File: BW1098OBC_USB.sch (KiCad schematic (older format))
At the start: 53 parts, among them J10 USB3.1 TYPEC 24P SMD RA, U5 USB Type-C Switch, U6 USB Type-C Port Control

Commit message: Update
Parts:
- C?: renamed from C31; symbol BW1098OBC_USB-SchDoc-rescue:GRM033R61A104KE15D- -> BW1098OBC_USB-cache:GRM033R61A104KE15D
- C?: renamed from C32; symbol BW1098OBC_USB-SchDoc-rescue:GRM033R61A104KE15D- -> BW1098OBC_USB-cache:GRM033R61A104KE15D
- C?: renamed from C33; symbol BW1098OBC_USB-SchDoc-rescue:GRM033R61A104KE15D- -> BW1098OBC_USB-cache:GRM033R61A104KE15D
- C?: renamed from C34; symbol BW1098OBC_USB-SchDoc-rescue:GRM033R61A104KE15D- -> BW1098OBC_USB-cache:GRM033R61A104KE15D
- C?: renamed from C36; symbol BW1098OBC_USB-SchDoc-rescue:GRM155R60J106ME15D- -> BW1098OBC_Power_Supply-cache:BW1098OBC_Power_Supply-SchDoc-rescue_GRM188R61A226ME15D-
- C?: renamed from C35; symbol BW1098OBC_USB-SchDoc-rescue:GRM155R60J106ME15D- -> BW1098OBC_Power_Supply-cache:BW1098OBC_Power_Supply-SchDoc-rescue_GRM188R61A226ME15D-
- C?: renamed from C29; symbol BW1098OBC_USB-SchDoc-rescue:GRM155R60J106ME15D- -> BW1098OBC_Power_Supply-cache:BW1098OBC_Power_Supply-SchDoc-rescue_GRM188R61A226ME15D-
- C?: renamed from C30; symbol BW1098OBC_USB-SchDoc-rescue:GRM155R60J106ME15D- -> BW1098OBC_Power_Supply-cache:BW1098OBC_Power_Supply-SchDoc-rescue_GRM188R61A226ME15D-
- J?: renamed from J10; symbol BW1098OBC_USB-SchDoc-rescue:105450-0101- -> BW1098OBC_USB-cache:105450-0101
- R?: renamed from R11; symbol BW1098OBC_USB-SchDoc-rescue:RC0402FR-1310KL- -> BW1098OBC_IMX378-rescue:RC0402FR-1310KL--BW1098OBC_IMX378-SchDoc-rescue
- R?: renamed from R12; symbol BW1098OBC_USB-SchDoc-rescue:RC0402FR-1310KL- -> BW1098OBC_IMX378-rescue:RC0402FR-1310KL--BW1098OBC_IMX378-SchDoc-rescue
- R?: renamed from R16; symbol BW1098OBC_USB-SchDoc-rescue:RC0402FR-1310KL- -> BW1098OBC_IMX378-rescue:RC0402FR-1310KL--BW1098OBC_IMX378-SchDoc-rescue
- R?: renamed from R14; symbol BW1098OBC_USB-SchDoc-rescue:RC0402FR-1310KL- -> BW1098OBC_IMX378-rescue:RC0402FR-1310KL--BW1098OBC_IMX378-SchDoc-rescue
- R?: renamed from R13; symbol BW1098OBC_USB-SchDoc-rescue:RC0402FR-1310KL- -> BW1098OBC_IMX378-rescue:RC0402FR-1310KL--BW1098OBC_IMX378-SchDoc-rescue
- R?: renamed from R21; symbol BW1098OBC_USB-SchDoc-rescue:RC0402FR-1310KL- -> BW1098OBC_IMX378-rescue:RC0402FR-1310KL--BW1098OBC_IMX378-SchDoc-rescue
- R?: renamed from R20; symbol BW1098OBC_USB-SchDoc-rescue:RC0402FR-1310KL- -> BW1098OBC_IMX378-rescue:RC0402FR-1310KL--BW1098OBC_IMX378-SchDoc-rescue
- R?: renamed from R19; symbol BW1098OBC_USB-SchDoc-rescue:RC0402FR-1310KL- -> BW1098OBC_IMX378-rescue:RC0402FR-1310KL--BW1098OBC_IMX378-SchDoc-rescue
- R?: renamed from R15; symbol BW1098OBC_USB-SchDoc-rescue:CRCW04021M80FKED- -> BW1098OBC_USB-cache:CRCW04021M80FKED
- R?: renamed from R17; symbol BW1098OBC_USB-SchDoc-rescue:CRCW04021M80FKED- -> BW1098OBC_USB-cache:CRCW04021M80FKED
- R?: renamed from R18; symbol BW1098OBC_USB-SchDoc-rescue:RC0402FR-1310KL- -> BW1098OBC_IMX378-rescue:RC0402FR-1310KL--BW1098OBC_IMX378-SchDoc-rescue
- TP?: renamed from TP23; value (none) -> ~; symbol BW1098OBC_USB-SchDoc-rescue:TEST_POINT- -> BW1098OBC_Power_Supply-cache:BW1098OBC_Power_Supply-SchDoc-rescue_TEST_POINT-
- TP?: renamed from TP22; value (none) -> ~; symbol BW1098OBC_USB-SchDoc-rescue:TEST_POINT- -> BW1098OBC_Power_Supply-cache:BW1098OBC_Power_Supply-SchDoc-rescue_TEST_POINT-
- TP?: renamed from TP21; value (none) -> ~; symbol BW1098OBC_USB-SchDoc-rescue:TEST_POINT- -> BW1098OBC_Power_Supply-cache:BW1098OBC_Power_Supply-SchDoc-rescue_TEST_POINT-
- TP?: renamed from TP19; value (none) -> ~; symbol BW1098OBC_USB-SchDoc-rescue:TEST_POINT- -> BW1098OBC_Power_Supply-cache:BW1098OBC_Power_Supply-SchDoc-rescue_TEST_POINT-
- U?: renamed from U5; symbol BW1098OBC_USB-SchDoc-rescue:HD3SS3212RKSR- -> BW1098OBC_USB-cache:HD3SS3212RKSR
- U?: renamed from U6; symbol BW1098OBC_USB-SchDoc-rescue:TUSB321RWBR- -> BW1098OBC_USB-cache:TUSB321RWBR
- renumbered 3V3_5 to 3V3_?, 3V3_4 to 3V3_?, 3V3_3 to 3V3_?, GND_88 to GND_?, GND_87 to GND_?, GND_86 to GND_?, GND_85 to GND_?, GND_84 to GND_?, GND_83 to GND_?, GND_82 to GND_?, GND_81 to GND_?, GND_80 to GND_?, GND_79 to GND_?, GND_78 to GND_?, GND_77 to GND_?, GND_76 to GND_?, GND_75 to GND_?, GND_74 to GND_?, VBUS_10 to VBUS_?, VBUS_9 to VBUS_?, VBUS_8 to VBUS_?, VBUS_7 to VBUS_?, VBUS_6 to VBUS_?, VBUS_5 to VBUS_?, VDD_5V_19 to VDD_5V_?, VDD_5V_18 to VDD_5V_?, VDD_5V_17 to VDD_5V_?
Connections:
- wire segments 138 -> 142

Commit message: Cleaned up some duplicates, started reorganizing and putting symbols into one luxonis library so the others can be deleted, added SOM Connector footprint
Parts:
- R? (x9): symbol BW1098OBC_IMX378-rescue:RC0402FR-1310KL--BW1098OBC_IMX378-SchDoc-rescue -> BW1098OBC_TopLevel-rescue:RC0402FR-1310KL--BW1098OBC_IMX378-SchDoc-rescue-BW1098OBC_IMX378-rescue
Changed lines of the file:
@@
 Connection ~ 13300 7600
 $Comp
-L BW1098OBC_IMX378-rescue:RC0402FR-1310KL--BW1098OBC_IMX378-SchDoc-rescue R?
+L BW1098OBC_TopLevel-rescue:RC0402FR-1310KL--BW1098OBC_IMX378-SchDoc-rescue-BW1098OBC_IMX378-rescue R?
 U 1 1 5FD52F8D
 P 12400 7300
@@
 $EndComp
 $Comp
-L BW1098OBC_IMX378-rescue:RC0402FR-1310KL--BW1098OBC_IMX378-SchDoc-rescue R?
+L BW1098OBC_TopLevel-rescue:RC0402FR-1310KL--BW1098OBC_IMX378-SchDoc-rescue-BW1098OBC_IMX378-rescue R?
 U 1 1 5FD52F82
 P 12400 7400
@@
 $EndComp
 $Comp
-L BW1098OBC_IMX378-rescue:RC0402FR-1310KL--BW1098OBC_IMX378-SchDoc-rescue R?
+L BW1098OBC_TopLevel-rescue:RC0402FR-1310KL--BW1098OBC_IMX378-SchDoc-rescue-BW1098OBC_IMX378-rescue R?
 U 1 1 5FD52F7A
 P 12400 7600
@@
 $EndComp
 $Comp
-L BW1098OBC_IMX378-rescue:RC0402FR-1310KL--BW1098OBC_IMX378-SchDoc-rescue R?
+L BW1098OBC_TopLevel-rescue:RC0402FR-1310KL--BW1098OBC_IMX378-SchDoc-rescue-BW1098OBC_IMX378-rescue R?
 U 1 1 5FD52F79
 P 12400 7700
@@
 $EndComp
 $Comp
-L BW1098OBC_IMX378-rescue:RC0402FR-1310KL--BW1098OBC_IMX378-SchDoc-rescue R?
+L BW1098OBC_TopLevel-rescue:RC0402FR-1310KL--BW1098OBC_IMX378-SchDoc-rescue-BW1098OBC_IMX378-rescue R?
 U 1 1 5FD52F78
 P 12400 6000
@@
 $EndComp
 $Comp
-L BW1098OBC_IMX378-rescue:RC0402FR-1310KL--BW1098OBC_IMX378-SchDoc-rescue R?
+L BW1098OBC_TopLevel-rescue:RC0402FR-1310KL--BW1098OBC_IMX378-SchDoc-rescue-BW1098OBC_IMX378-rescue R?
 U 1 1 5FD52F77
 P 12400 6600
@@
 $EndComp
 $Comp
-L BW1098OBC_IMX378-rescue:RC0402FR-1310KL--BW1098OBC_IMX378-SchDoc-rescue R?
+L BW1098OBC_TopLevel-rescue:RC0402FR-1310KL--BW1098OBC_IMX378-SchDoc-rescue-BW1098OBC_IMX378-rescue R?
 U 1 1 5FD52F76
 P 12400 6700
@@
 $EndComp
 $Comp
-L BW1098OBC_IMX378-rescue:RC0402FR-1310KL--BW1098OBC_IMX378-SchDoc-rescue R?
+L BW1098OBC_TopLevel-rescue:RC0402FR-1310KL--BW1098OBC_IMX378-SchDoc-rescue-BW1098OBC_IMX378-rescue R?
 U 1 1 5FD52F75
 P 11400 5000
@@
 $EndComp
 $Comp
-L BW1098OBC_IMX378-rescue:RC0402FR-1310KL--BW1098OBC_IMX378-SchDoc-rescue R?
+L BW1098OBC_TopLevel-rescue:RC0402FR-1310KL--BW1098OBC_IMX378-SchDoc-rescue-BW1098OBC_IMX378-rescue R?
 U 1 1 5FD52F74
 P 4300 1400

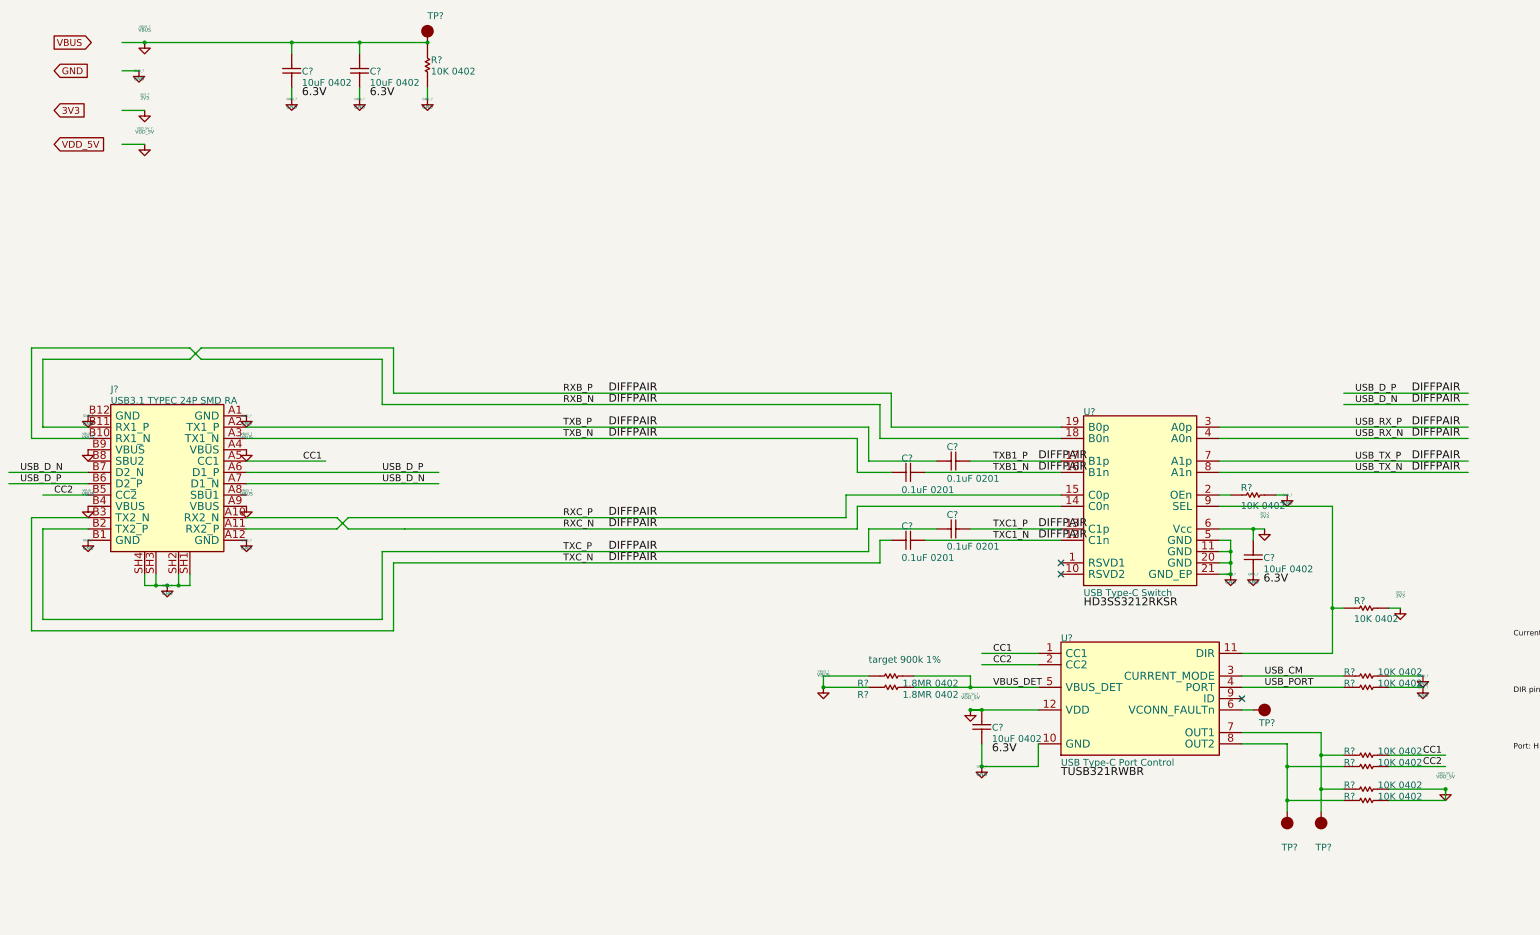
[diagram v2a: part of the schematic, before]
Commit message: More deletion of corrupted or duplicate files, added footprints and associations for mounting holes and 30 pin connector
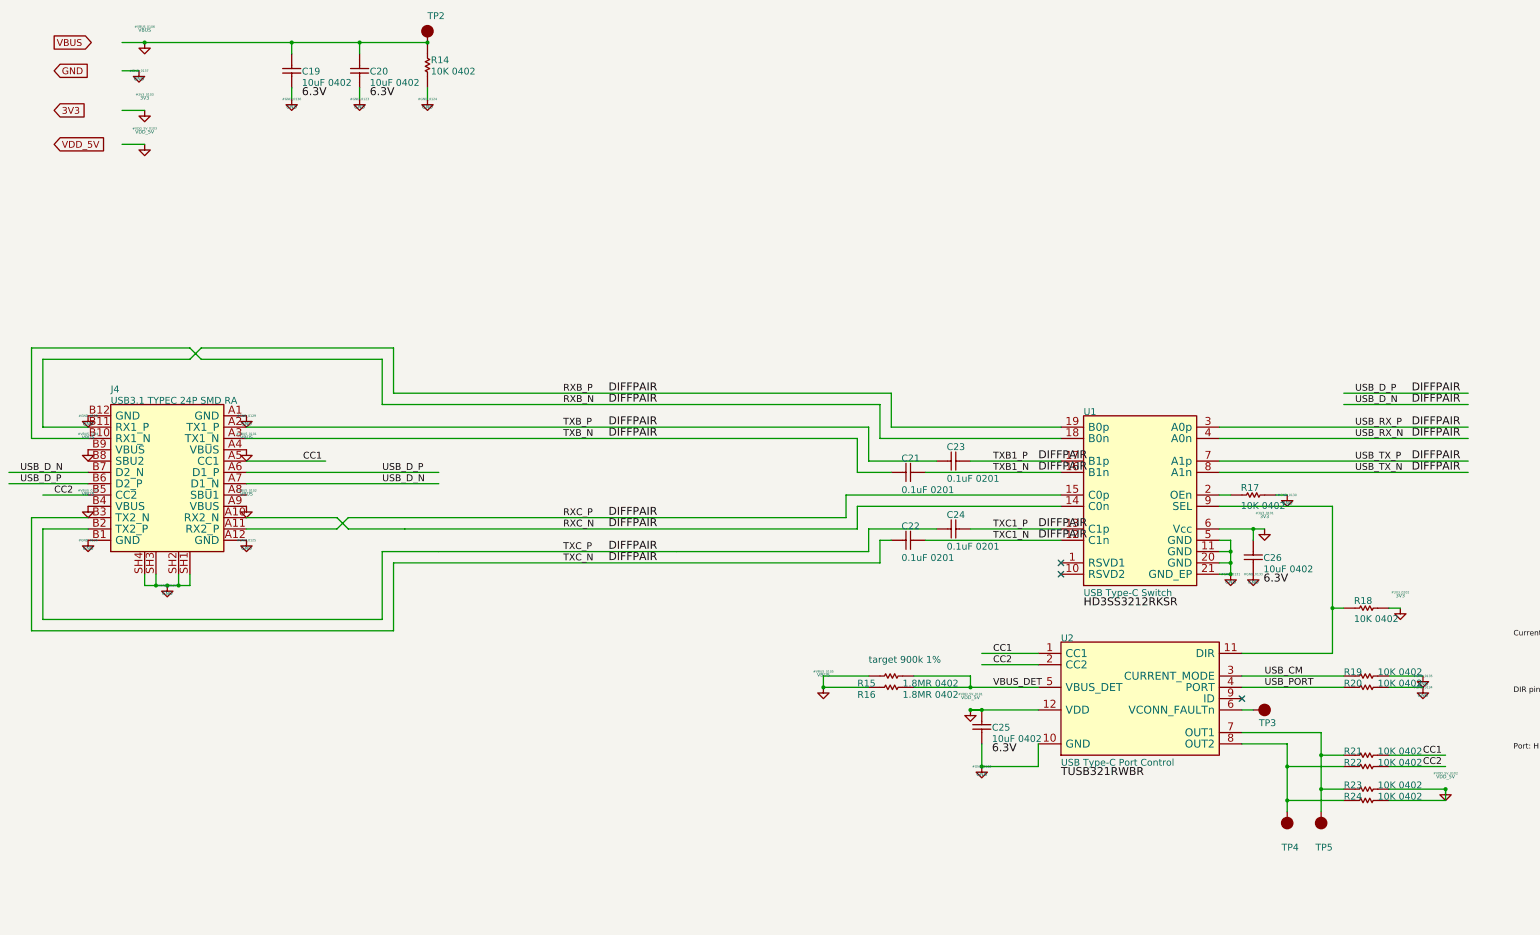
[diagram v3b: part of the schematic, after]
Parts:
- removed 3V3_? (x3): 3V3, symbol power:GND
- removed GND_? (x15): GND, symbol power:GND
- removed VBUS_? (x6): VBUS, symbol power:GND
- removed VDD_5V_? (x3): VDD_5V, symbol power:GND
- gave numbers to parts that had none: 26
